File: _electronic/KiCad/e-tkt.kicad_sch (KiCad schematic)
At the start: 0 parts

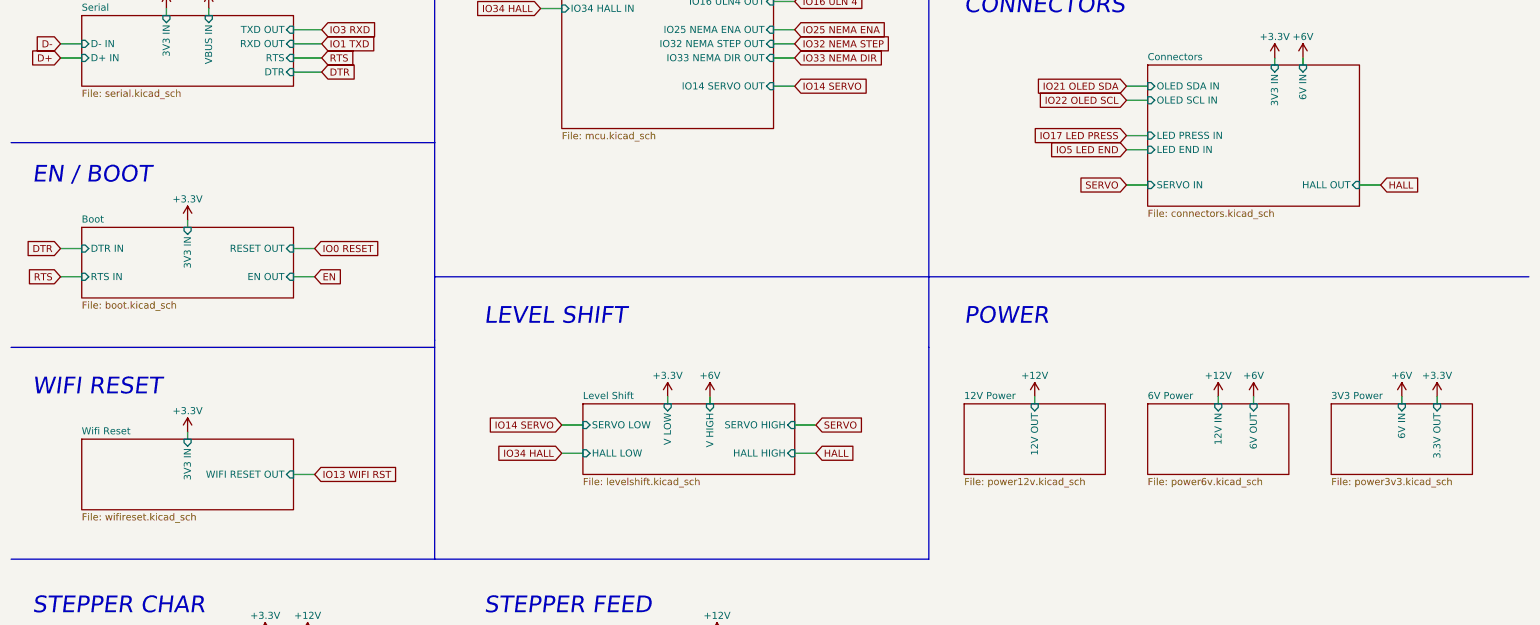
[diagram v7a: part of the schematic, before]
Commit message: added buzzer
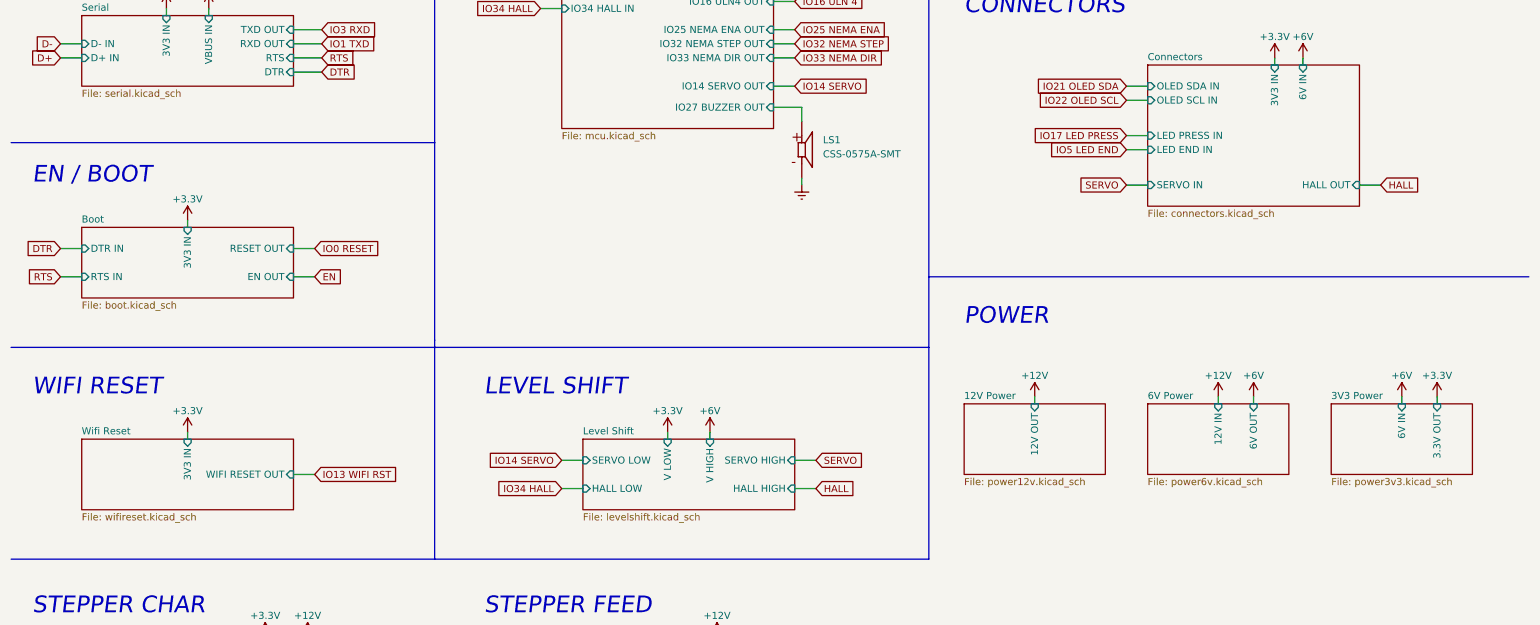
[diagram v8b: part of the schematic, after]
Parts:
- added LS1: CSS-0575A-SMT, SnapEDA Library:CUI_CSS-0575A-SMT, symbol CSS-0575A-SMT:CSS-0575A-SMT
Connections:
- new net GNDREF: LS1.2
- new net MCU/IO27 BUZZER OUT: LS1.1
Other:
- sheet MCU ports: added IO27 BUZZER OUT; removed none
